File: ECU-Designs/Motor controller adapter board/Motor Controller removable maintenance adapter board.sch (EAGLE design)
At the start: 5 parts, among them X1 MINIFIT_5566-6

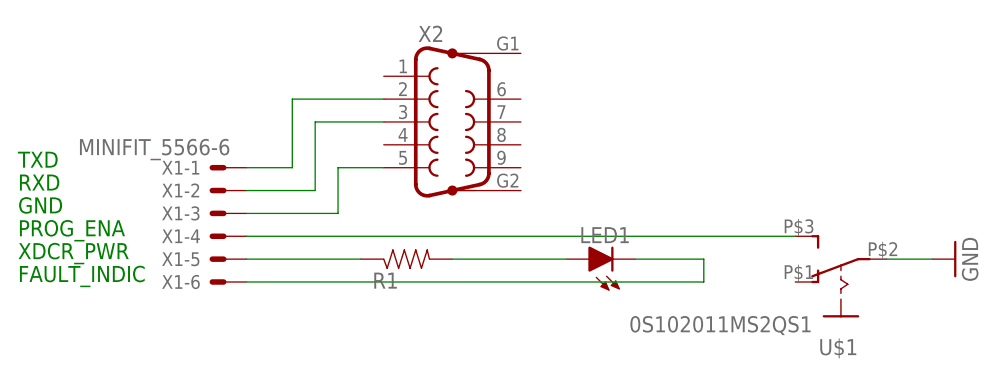
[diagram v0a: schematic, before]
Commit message: Updated motor controller board switch
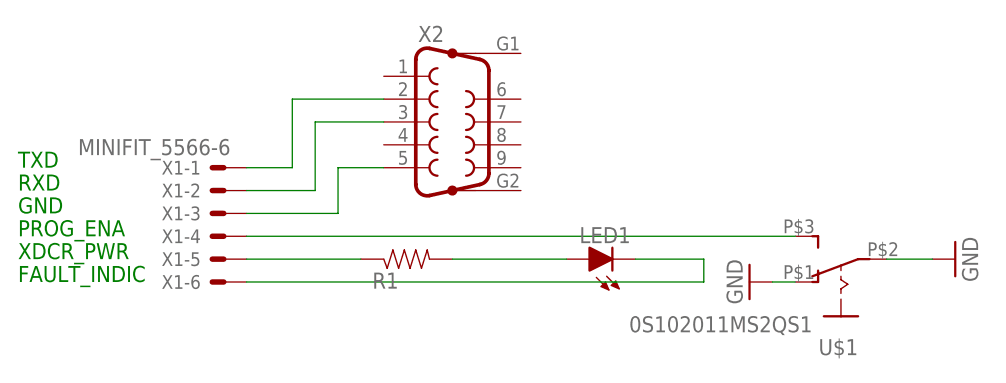
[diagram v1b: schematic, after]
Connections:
- net GND: now also U$1.O
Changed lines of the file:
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@@
 <part name="X2" library="con-subd" deviceset="F09HP" device=""/>
 <part name="U$1" library="HyTechDevices" deviceset="0S102011MS2QS1" device=""/>
+<part name="GND2" library="HyTechSymbols" deviceset="GND" device=""/>
 </parts>
 <sheets>
@@
 <instance part="X2" gate="G$1" x="-22.86" y="68.58"/>
 <instance part="U$1" gate="G$1" x="20.32" y="50.8" rot="R90"/>
+<instance part="GND2" gate="1" x="10.16" y="50.8" rot="R270"/>
 </instances>
 <busses>
@@
 <pinref part="U$1" gate="G$1" pin="P"/>
 </segment>
+<segment>
+<pinref part="U$1" gate="G$1" pin="O"/>
+<pinref part="GND2" gate="1" pin="GND"/>
+<wire x1="12.7" y1="50.8" x2="15.24" y2="50.8" width="0.1524" layer="91"/>
+</segment>
 </net>

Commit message: Move bms header board, add ltc6820 breakout, fix mc adapter board for manufacturing
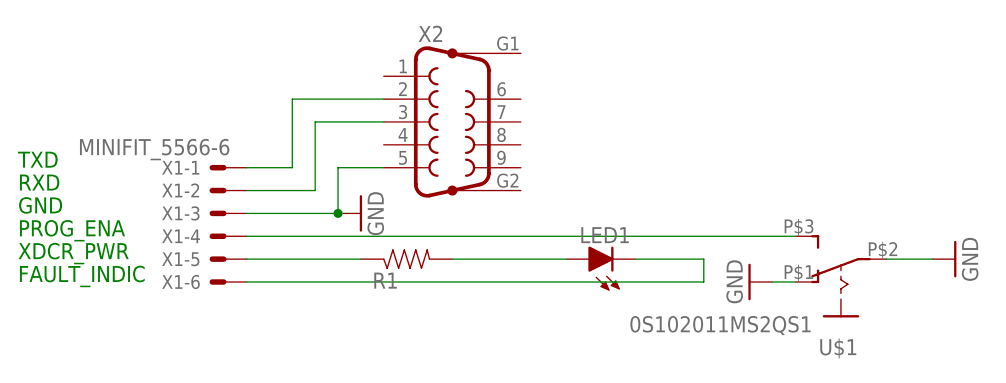
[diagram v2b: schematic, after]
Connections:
- removed net N$8: X1-3.S, X2.5
- net GND: now also X1-3.S, X2.5
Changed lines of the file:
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@@
 <?xml version="1.0" encoding="utf-8"?>
 <!DOCTYPE eagle SYSTEM "eagle.dtd">
-<eagle version="7.7.0">
+<eagle version="8.1.0">
 <drawing>
 <settings>
@@
 <part name="U$1" library="HyTechDevices" deviceset="0S102011MS2QS1" device=""/>
 <part name="GND2" library="HyTechSymbols" deviceset="GND" device=""/>
+<part name="GND3" library="HyTechSymbols" deviceset="GND" device=""/>
 </parts>
 <sheets>
@@
 <instance part="U$1" gate="G$1" x="20.32" y="50.8" rot="R90"/>
 <instance part="GND2" gate="1" x="10.16" y="50.8" rot="R270"/>
+<instance part="GND3" gate="1" x="-33.02" y="58.42" rot="R90"/>
 </instances>
 <busses>
@@
 <wire x1="12.7" y1="50.8" x2="15.24" y2="50.8" width="0.1524" layer="91"/>
 </segment>
+<segment>
+<pinref part="X1" gate="-3" pin="S"/>
+<wire x1="-45.72" y1="58.42" x2="-35.56" y2="58.42" width="0.1524" layer="91"/>
+<wire x1="-35.56" y1="58.42" x2="-35.56" y2="63.5" width="0.1524" layer="91"/>
+<pinref part="X2" gate="G$1" pin="5"/>
+<wire x1="-35.56" y1="63.5" x2="-30.48" y2="63.5" width="0.1524" layer="91"/>
+<pinref part="GND3" gate="1" pin="GND"/>
+<junction x="-35.56" y="58.42"/>
+</segment>
 </net>
 <net name="N$6" class="0">
@@
 </segment>
 </net>
-<net name="N$8" class="0">
-<segment>
-<pinref part="X1" gate="-3" pin="S"/>
-<wire x1="-45.72" y1="58.42" x2="-35.56" y2="58.42" width="0.1524" layer="91"/>
-<wire x1="-35.56" y1="58.42" x2="-35.56" y2="63.5" width="0.1524" layer="91"/>
-<pinref part="X2" gate="G$1" pin="5"/>
-<wire x1="-35.56" y1="63.5" x2="-30.48" y2="63.5" width="0.1524" layer="91"/>
-</segment>
-</net>
